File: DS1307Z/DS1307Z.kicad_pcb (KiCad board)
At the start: 2 copper layers, 25.4 x 17.8 mm, 20 parts, among them J1 Conn_01x06, J2 Conn_01x04, J4 Conn_01x04, U1 DS1307ZN+, Y1 32.768kHz

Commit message: Soldermask width adjusted
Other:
- rule solder_mask_min_width: 0.1 -> 0.05
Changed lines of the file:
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@@
     (pad_drill 0)
     (pad_to_mask_clearance 0)
-    (solder_mask_min_width 0.1)
+    (solder_mask_min_width 0.05)
     (aux_axis_origin 0 0)
     (visible_elements 7FFFFFFF)

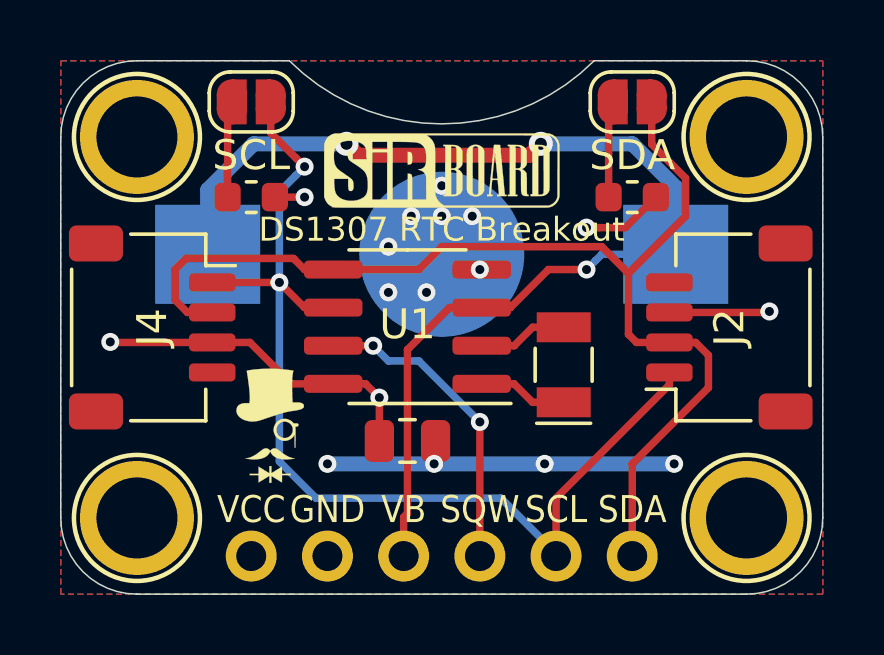
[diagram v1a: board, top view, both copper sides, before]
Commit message: DS1307 Update
Bypass Caps Added to Crystal
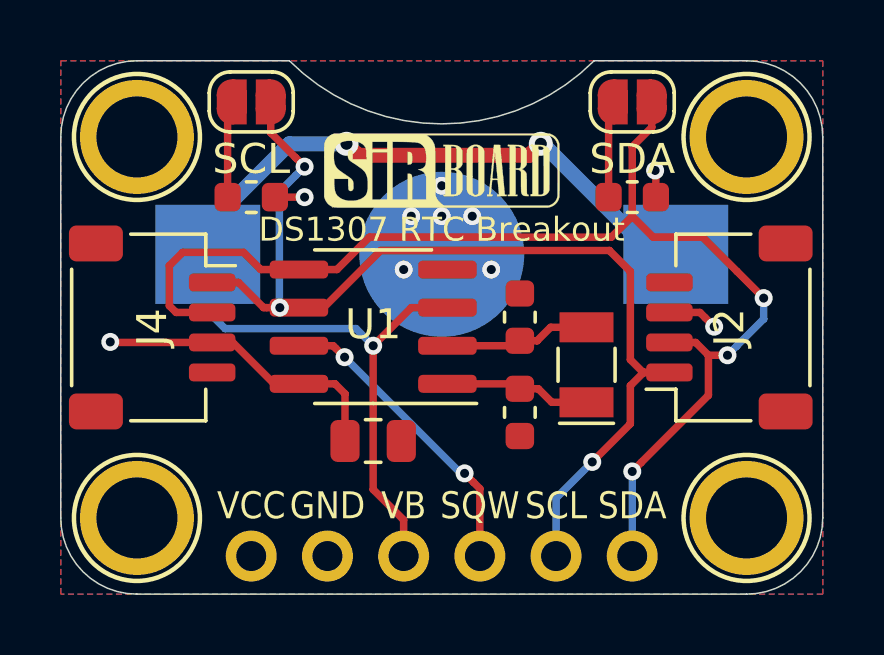
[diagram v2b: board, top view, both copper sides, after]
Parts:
- removed the G*** at (59.6, 36.7)
- added C2: 12pF, Capacitor_SMD:C_0603_1608Metric, F.Cu at (67.9, 36.3)
- added C3: 12pF, Capacitor_SMD:C_0603_1608Metric, F.Cu at (67.9, 33.1)
- moved C1 1.14 mm to (63.0, 37.2)
- moved U1 1.14 mm to (63.0, 33.4)
- moved Y1 0.76 mm to (70.1, 34.7)
- renumbered CR1220 to BT1
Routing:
- net GND: track 11.6 -> 0.00 mm, vias 12 -> 6
- net VCC: track 18.3 -> 13.7 mm, vias 5 -> 4
- net SDA: track 38.2 -> 41.3 mm, vias 0 -> 3
- net Net-(C3-Pad1): track 2.99 -> 4.89 mm
- net Net-(C2-Pad1): track 2.99 -> 4.89 mm
- net VBAT: track 38.8 -> 37.9 mm
- net SCL: track 35.4 -> 35.7 mm, vias 2 -> 3
